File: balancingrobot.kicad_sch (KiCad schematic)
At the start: 34 parts, among them J1 Conn_01x04, J12 Conn_01x02, J4 Conn_01x02, J5 Conn_01x22, J6 Conn_01x22, J7 Conn_01x22, J8 Conn_01x02, J9 Conn_01x06, SW1 SW_Push, SW2 SW_Push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

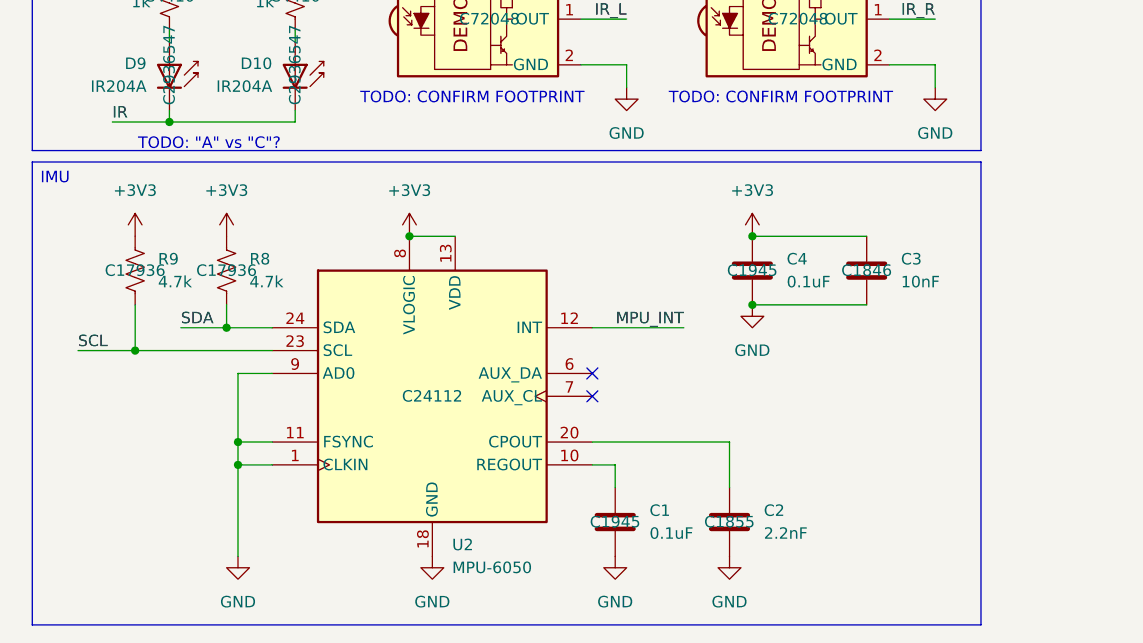
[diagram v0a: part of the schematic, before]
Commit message: Remove MPU6050
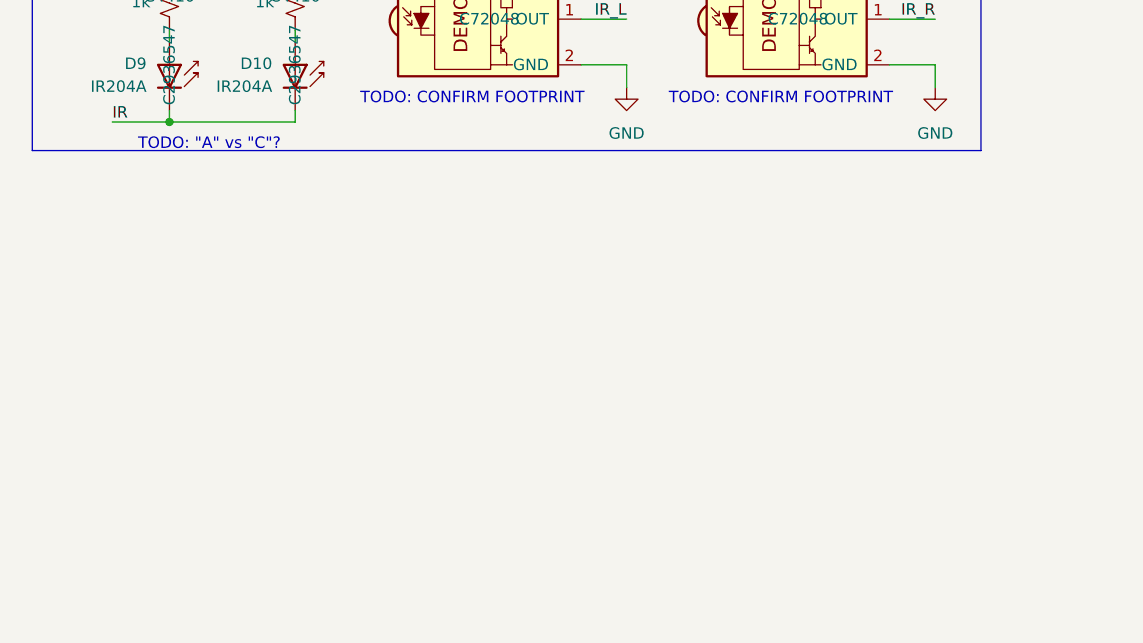
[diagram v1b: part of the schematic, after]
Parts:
- removed C1, C4: 0.1uF, Capacitor_SMD:C_1206_3216Metric, symbol Device:C
- removed C2: 2.2nF, Capacitor_SMD:C_1206_3216Metric, symbol Device:C
- removed C3: 10nF, Capacitor_SMD:C_1206_3216Metric, symbol Device:C
- removed R8, R9: 4.7k, Resistor_SMD:R_1206_3216Metric, symbol Device:R_US
- removed U2: MPU-6050, Sensor_Motion:InvenSense_QFN-24_4x4mm_P0.5mm, symbol Sensor_Motion:MPU-6050
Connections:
- no-connect marks 10 -> 8
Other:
- note removed: "IMU"

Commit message: Update readme
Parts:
- added J14, J15: Conn_01x08, Connector_PinSocket_2.54mm:PinSocket_1x08_P2.54mm_Vertical, symbol Connector_Generic:Conn_01x08
- added J16, J17: Conn_01x15, Connector_PinSocket_2.54mm:PinSocket_1x15_P2.54mm_Vertical, symbol Connector_Generic:Conn_01x15
- J5, J6, J7: JLC P/N C7430378 -> C725954
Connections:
- no-connect marks 8 -> 54
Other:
- note added: "These are shims to get JLC to assemble the female headers for the socketed components"
- note removed: "TODO: CONFIRM FOOTPRINT"
